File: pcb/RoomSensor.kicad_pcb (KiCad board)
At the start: 2 copper layers, 70 x 32 mm, 63 parts, among them J1 FH34SRJ-24S-0.5SH50, J2 USB_C_Receptacle_PowerOnly_6P, J3 programming, J4 external supply, Q1 SI1308EDL-T1-GE3, SW1 SW_Push, U1 ESP32-WROOM-32D, U2 DW01-P, U3 CEG8205A, U4 RT9080-33GJ5, U5 TP4056, U6 SCD40-D-R1, U7 SHT31-DIS, U8 BME680

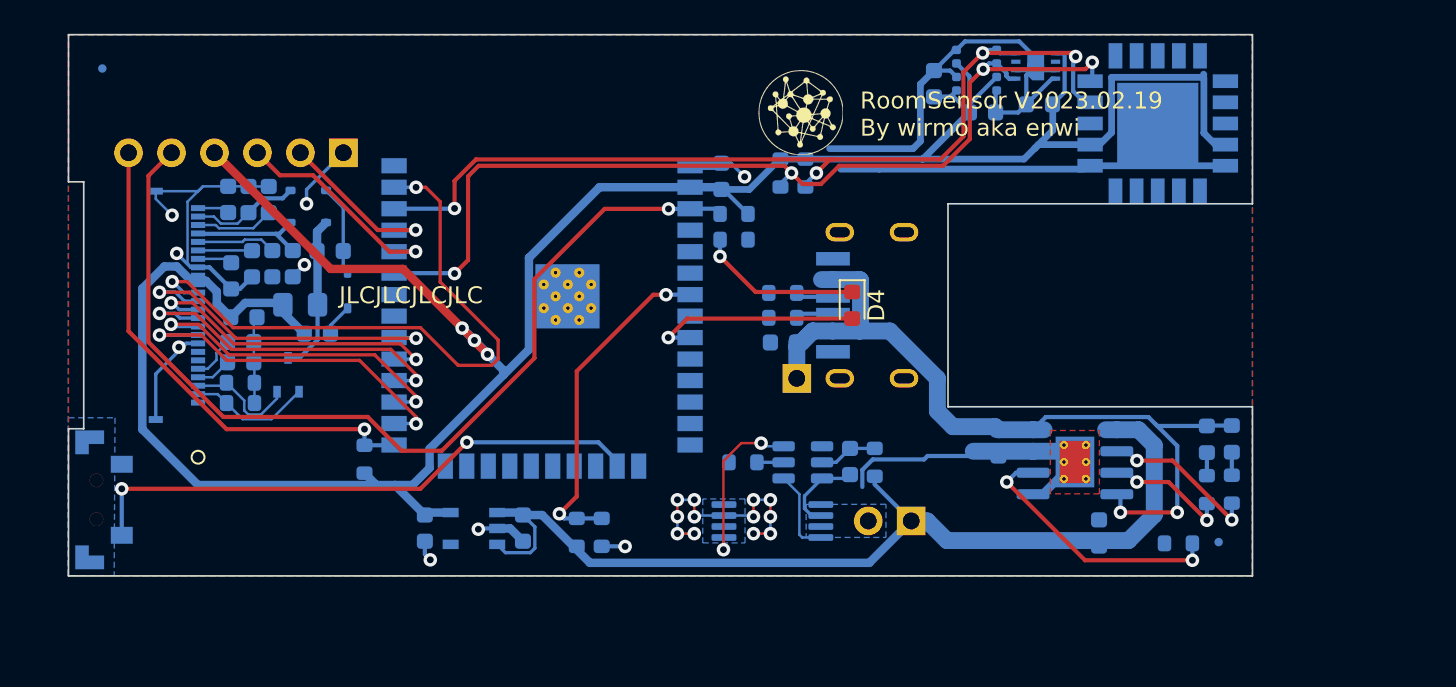
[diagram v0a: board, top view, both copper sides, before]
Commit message: Increase PCB size and fix EPD pinout
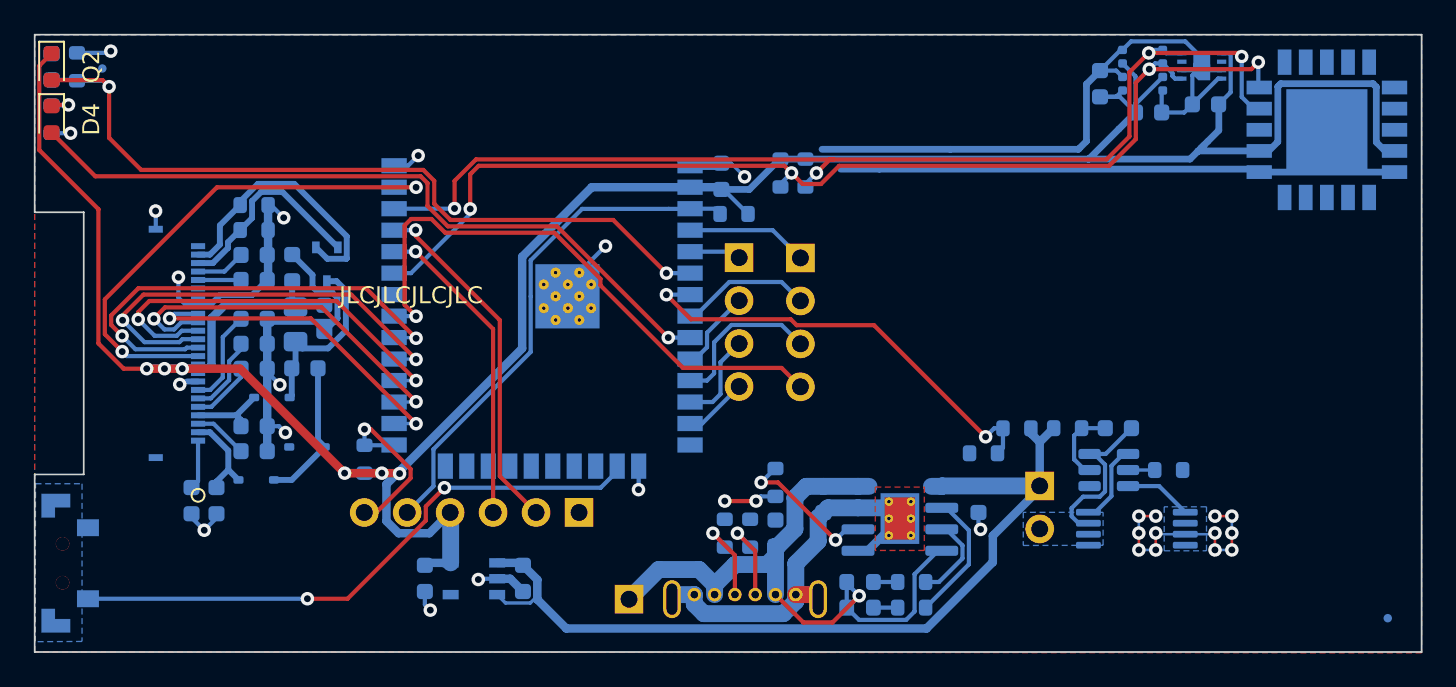
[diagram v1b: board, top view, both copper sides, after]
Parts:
- removed Ref**: Val**, Symbols_Custom:enwi_5mm
- added C15: 100n, Capacitor_SMD:C_0603_1608Metric, B.Cu at (-1.00, 1.90)
- added J5: Conn_01x04_Pin, Connector_PinHeader_2.54mm:PinHeader_1x04_P2.54mm_Vertical, B.Cu at (39.6, 13.2)
- added J6: Conn_01x04_Pin, Connector_PinHeader_2.54mm:PinHeader_1x04_P2.54mm_Vertical, B.Cu at (43.3, 13.2)
- added Q2: ALS-PT19-315C/L177/TR8, LED_SMD:LED_0603_1608Metric, F.Cu at (-1.00, 1.90)
- added R17: R_Small, Resistor_SMD:R_0603_1608Metric, B.Cu at (0.50, 1.90)
- C1, C10, C2, C3, C4, C5, C6, C7, C8, C9: value 1uF -> 1u
- C11, C12: value 4.7uF -> 4.7u
- C13: value 10uF -> 10u
- C16: value 0.1u -> 100n
- FID2: footprint Fiducial:Fiducial_0.5mm_Mask1mm -> Fiducial:Fiducial_0.5mm_Mask1.5mm
- J2: footprint Custom:TYPE-C-31-M-17_B -> Custom:TYPE-C 6P LCH10.0
- L1: value L_Small -> 68u
- moved D4 48.6 mm to (-1.00, 5.00)
- moved R11 41.0 mm to (-1.00, 5.00), turned to 90 degrees
- moved R9 26.7 mm to (56.1, 23.3), turned to 0 degrees
- moved J3 25.4 mm to (30.2, 28.2)
- moved R12 25.2 mm to (65.0, 25.7), turned to 0 degrees
- moved D6 24.1 mm to (46.8, 33.9), turned to 180 degrees
- moved R14 24.1 mm to (41.8, 26.5), turned to 90 degrees
- moved R10 23.1 mm to (54.1, 24.8), turned to 0 degrees
- moved D5 22.2 mm to (46.8, 32.4), turned to 180 degrees
- moved U3 21.6 mm to (63.2, 29.2), turned to 0 degrees
- moved R16 20.2 mm to (49.9, 33.9), turned to 180 degrees
- moved R15 18.3 mm to (49.9, 32.4), turned to 180 degrees
- moved J2 18.1 mm to (40.0, 31.5), turned to 0 degrees
- moved U2 18.1 mm to (61.5, 25.7), turned to 180 degrees
- moved C1 17.9 mm to (7.28, 27.6), turned to -90 degrees
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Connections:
- J1 pad 1: unconnected-(J1-Pad1) -> Net-(C1-Pad1)
- J1 pad 10: ESP_IO16 -> +3V3
- J1 pad 11: DC -> ESP_IO23
- J1 pad 12: CS -> CLK
- J1 pad 13: CLK -> CS
- J1 pad 14: ESP_IO23 -> DC
- J1 pad 15: +3V3 -> ESP_IO16
- J1 pad 16: +3V3 -> BUSY
- J1 pad 18: Net-(C4-Pad1) -> unconnected-(J1-Pad18)
- J1 pad 19: Net-(C9-Pad1) -> unconnected-(J1-Pad19)
- J1 pad 2: Net-(Q1-G) -> Net-(D2-A)
- J1 pad 20: Net-(C3-Pad1) -> Net-(C6-Pad1)
- J1 pad 21: Net-(D3-K) -> Net-(C10-Pad1)
- J1 pad 22: Net-(C2-Pad1) -> Net-(Q1-S)
- J1 pad 23: Net-(D2-A) -> Net-(Q1-G)
- J1 pad 24: Net-(C1-Pad1) -> unconnected-(J1-Pad24)
- J1 pad 3: Net-(Q1-S) -> Net-(C2-Pad1)
- J1 pad 4: Net-(C10-Pad1) -> Net-(D3-K)
- J1 pad 5: Net-(C6-Pad1) -> Net-(C3-Pad1)
- J1 pad 6: unconnected-(J1-Pad6) -> Net-(C9-Pad1)
- J1 pad 7: unconnected-(J1-Pad7) -> Net-(C4-Pad1)
- J1 pad 9: BUSY -> +3V3
- SW1 pad 3: (no net) -> -BATT
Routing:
- net ESP_IO34: track 0.00 -> 48.6 mm, vias 0 -> 2
- net -BATT: track 133.2 -> 170.7 mm, vias 21 -> 30
- net ESP_IO19: track 0.00 -> 34.9 mm, vias 0 -> 1
- net ESP_IO33: track 12.6 -> 43.6 mm
- net ESP_EN: track 57.0 -> 30.5 mm, vias 1 -> 0
- net ESP_IO0: track 29.6 -> 10.5 mm
- net +3V3: track 159.7 -> 172.1 mm, vias 3 -> 6
- net ESP_TX: track 9.99 -> 20.9 mm
- net ESP_IO22: track 55.3 -> 65.5 mm
- net ESP_IO26: track 0.00 -> 9.43 mm
- net Net-(Q1-G): track 7.26 -> 16.2 mm
- net ESP_IO21: track 57.2 -> 65.7 mm
- net +5V: track 49.2 -> 41.4 mm, vias 2 -> 1
- net ESP_IO32: track 0.00 -> 7.82 mm
- net Net-(D4-K): track 9.68 -> 2.04 mm
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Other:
- board size 70 x 32 mm -> 82 x 36.5 mm
- board text added: "IO 19|14"
- board text added: "IO 26|27"
- board text added: "IO 32|25"
- board text added: "IO 36|39"
- board text added: "RoomSensor V2023.02.25 By wirmo aka enwi"
- board text removed: "3V3"
- board text removed: "EN"
- board text removed: "GND"
- board text removed: "IO0"
- board text removed: "RX"
- board text removed: "RoomSensor V2023.02.19 By wirmo aka enwi"
- board text removed: "TX"

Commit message: Fix low power issues
- Fix spurious EPD wakeups by adding pull-up to EPD reset line
- Reduce power consumption by switching sensors off with mosfet
- Connect button to reset to reduce power by not needing rtc gpio
- Add solder jumper for silent boot
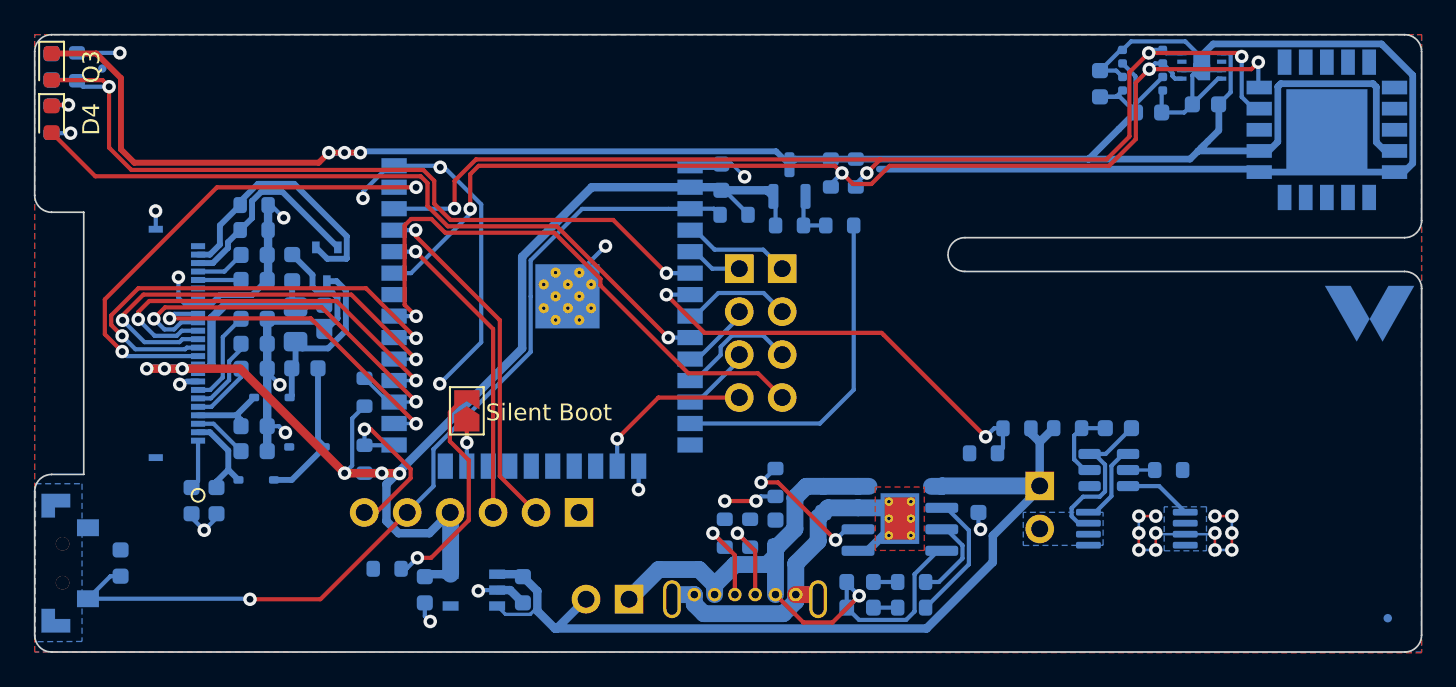
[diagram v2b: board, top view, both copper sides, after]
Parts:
- removed the J4 at (33.1, 33.4)
- added C15: 100n, Capacitor_SMD:C_0603_1608Metric, B.Cu at (3.08, 31.2)
- added J6: Conn_01x02_Pin, Connector_PinHeader_2.54mm:PinHeader_1x02_P2.54mm_Vertical, B.Cu at (33.1, 33.4)
- added JP1: silent boot, Jumper:SolderJumper-2_P1.3mm_Open_TrianglePad1.0x1.5mm, F.Cu at (23.6, 22.2)
- added Q2: AO3401A, Package_TO_SOT_SMD:SOT-23, B.Cu at (42.6, 8.62)
- added R15: 10k, Resistor_SMD:R_0603_1608Metric, B.Cu at (18.8, 31.6)
- added R5: 10k, Resistor_SMD:R_0603_1608Metric, B.Cu at (17.5, 21.1)
- added R6: 1k, Resistor_SMD:R_0603_1608Metric, B.Cu at (45.6, 11.3)
- added R7: 10k, Resistor_SMD:R_0603_1608Metric, B.Cu at (42.6, 11.3)
- added REF**: wirmo_small, Symbols_Custom:wirmo_small, B.Cu at (76.9, 16.5)
- FID1: footprint Fiducial:Fiducial_0.5mm_Mask1mm -> Fiducial:Fiducial_0.5mm_Mask1.5mm
- R21: renamed from R17; value R_Small -> 1k5
- moved R11 2.98 mm to (45.1, 8.18)
- moved R8 2.98 mm to (46.5, 8.18)
- moved J5 1.25 mm to (42.2, 13.8)
- moved U4 0.67 mm to (24.0, 32.8)
- moved C17 0.67 mm to (26.9, 32.8)
- moved C20 0.67 mm to (21.1, 32.8)
- moved J4 0.65 mm to (39.7, 13.8)
- moved C14 0.05 mm to (38.6, 8.43)
- moved R10 0.05 mm to (39.4, 10.7), turned to 180 degrees
- renumbered C15 to C21, C21 to C22, C22 to C23, C23 to C24, J5 to J4, J6 to J5, Q2 to Q3, R7 to R10, R8 to R11, R9 to R12, R10 to R13, R11 to R14, R12 to R16, R13 to R17, R14 to R18, R15 to R19, R16 to R20, R5 to R8, R6 to R9
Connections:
- C22 pad 1: +3V3 -> +3V3Sensors
- C23 pad 1: +3V3 -> +3V3Sensors
- C24 pad 1: +3V3 -> +3V3Sensors
- J4 pad 4: ESP_IO14 -> ESP_IO13
- Q3 pad 1: +3V3 -> +3V3Sensors
- R10 pad 1: ESP_EN -> +3V3
- R10 pad 2: +3V3 -> ESP_EN
- R11 pad 2: +3V3 -> +3V3Sensors
- R8 pad 2: +3V3 -> +3V3Sensors
- SW1 pad 2: ESP_IO13 -> ESP_EN
- SW1 pad 3: -BATT -> (no net)
- U1 pad 23: unconnected-(U1-IO15-Pad23) -> ESP_IO15
- U6 pad 19: +3V3 -> +3V3Sensors
- U6 pad 7: +3V3 -> +3V3Sensors
- U7 pad 5: +3V3 -> +3V3Sensors
- U8 pad 2: +3V3 -> +3V3Sensors
- U8 pad 6: +3V3 -> +3V3Sensors
- U8 pad 8: +3V3 -> +3V3Sensors
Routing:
- net +3V3Sensors: track 0.00 -> 115.9 mm, vias 0 -> 3
- net +3V3: track 172.1 -> 90.0 mm
- net ESP_IO13: track 35.6 -> 10.1 mm, vias 2 -> 1
- net ESP_EN: track 30.5 -> 54.1 mm, vias 0 -> 1
- net -BATT: track 170.7 -> 188.1 mm, vias 30 -> 32
- net ESP_IO14: track 3.81 -> 20.2 mm
- net Net-(JP1-B): track 0.00 -> 13.4 mm, vias 0 -> 1
- net Net-(Q2-G): track 0.00 -> 3.09 mm
- net ESP_IO15: track 0.00 -> 2.55 mm, vias 0 -> 1
- net ESP_IO16: track 22.5 -> 24.9 mm
- net ESP_IO26: track 9.43 -> 7.30 mm
- net ESP_IO32: track 7.82 -> 6.47 mm
- net ESP_IO27: track 5.43 -> 4.26 mm
- net +BATT: track 54.9 -> 55.7 mm
- net ESP_SEN_VP: track 7.20 -> 6.39 mm
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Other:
- outline, holes or cut-outs redrawn
- board text added: "0"
- board text added: "BV"
- board text added: "EN"
- board text added: "G"
- board text added: "IO 19|16"
- board text added: "RX"
- board text added: "RoomSensor V2023.04.01 by wirmo aka enwi"
- board text added: "Silent Boot"
- board text added: "TX"
- board text added: "V"
- board text removed: "IO 19|14"
- board text removed: "RoomSensor V2023.02.25 By wirmo aka enwi"

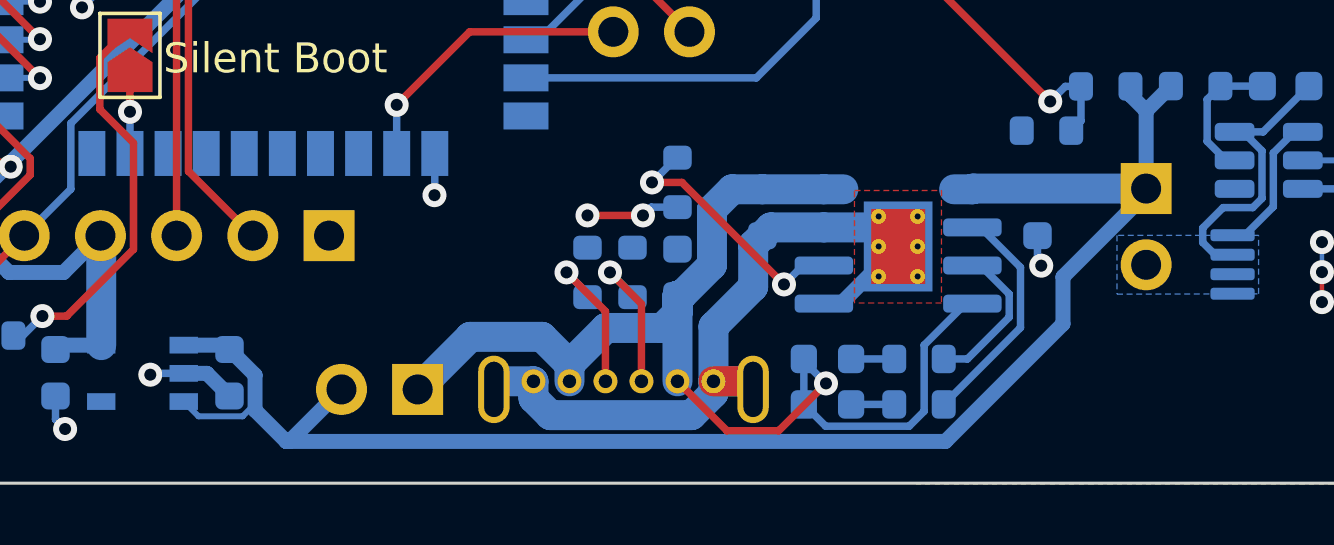
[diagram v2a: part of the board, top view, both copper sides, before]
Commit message: Replace b- net with -Battery
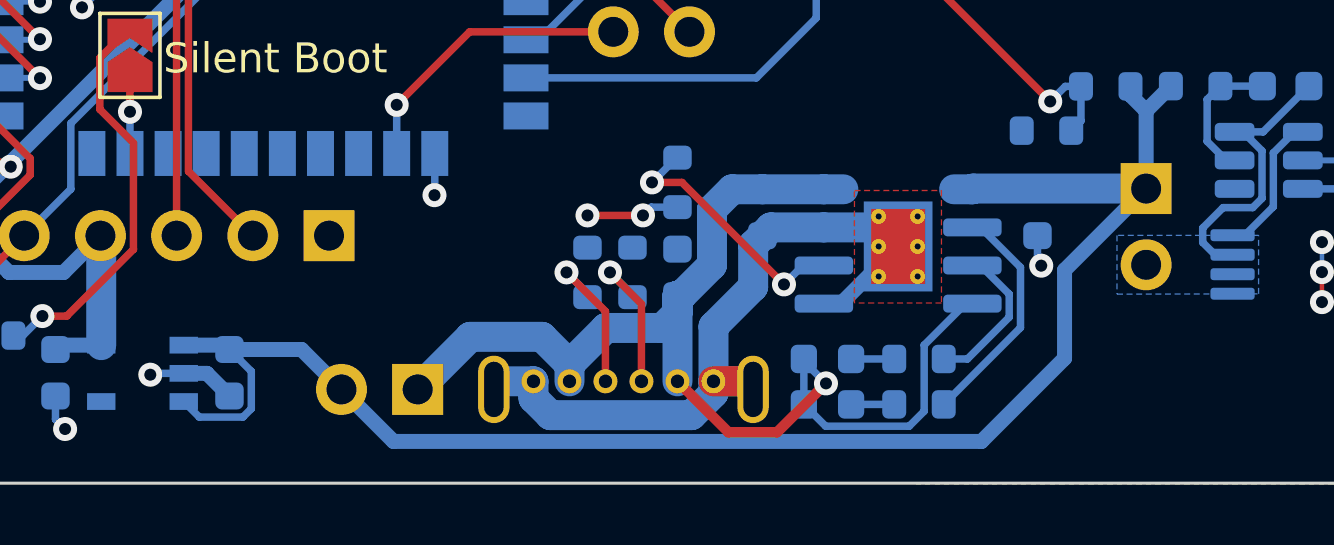
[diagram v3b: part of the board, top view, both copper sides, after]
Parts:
- R12, R13: value 47k -> 1M
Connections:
- BT1 pad 2: b- -> -BATT
- C1 pad 2: -BATT -> GND
- C10 pad 2: -BATT -> GND
- C12 pad 1: -BATT -> GND
- C13 pad 1: -BATT -> GND
- C14 pad 2: -BATT -> GND
- C15 pad 2: -BATT -> GND
- C16 pad 1: b- -> -BATT
- C17 pad 2: -BATT -> GND
- C18 pad 2: -BATT -> GND
- C19 pad 2: -BATT -> GND
- C2 pad 2: -BATT -> GND
- C20 pad 2: -BATT -> GND
- C21 pad 2: -BATT -> GND
- C22 pad 2: -BATT -> GND
- C23 pad 2: -BATT -> GND
- C24 pad 2: -BATT -> GND
- C3 pad 2: -BATT -> GND
- C4 pad 2: -BATT -> GND
- C5 pad 2: -BATT -> GND
- C6 pad 2: -BATT -> GND
- C7 pad 2: -BATT -> GND
- C8 pad 2: -BATT -> GND
- C9 pad 2: -BATT -> GND
- D1 pad 1: -BATT -> GND
- J1 pad 17: -BATT -> GND
- J1 pad 25: -BATT -> GND
- J1 pad 26: -BATT -> GND
- J1 pad 8: -BATT -> GND
- J2 pad A12: -BATT -> GND
- J2 pad S1: -BATT -> GND
- J3 pad 1: -BATT -> GND
- R1 pad 2: -BATT -> GND
- R13 pad 1: -BATT -> GND
- R14 pad 1: -BATT -> GND
- R15 pad 2: -BATT -> GND
- R16 pad 2: -BATT -> GND
- R18 pad 1: -BATT -> GND
- R2 pad 2: -BATT -> GND
- R21 pad 2: -BATT -> GND
- R3 pad 1: -BATT -> GND
- R4 pad 1: -BATT -> GND
- SW1 pad 1: -BATT -> GND
- U1 pad 1: -BATT -> GND
- U1 pad 15: -BATT -> GND
- U1 pad 38: -BATT -> GND
- U1 pad 39: -BATT -> GND
- U2 pad 6: b- -> -BATT
- U3 pad 2: b- -> -BATT
- U3 pad 3: b- -> -BATT
- U3 pad 6: -BATT -> GND
- U3 pad 7: -BATT -> GND
- U4 pad 2: -BATT -> GND
- U5 pad 1: -BATT -> GND
- U5 pad 3: -BATT -> GND
- U5 pad 9: -BATT -> GND
- U6 pad 20: -BATT -> GND
- U6 pad 21: -BATT -> GND
- U6 pad 6: -BATT -> GND
- U7 pad 2: -BATT -> GND
- U7 pad 7: -BATT -> GND
- U7 pad 8: -BATT -> GND
- U7 pad 9: -BATT -> GND
- U8 pad 1: -BATT -> GND
- U8 pad 5: -BATT -> GND
- U8 pad 7: -BATT -> GND
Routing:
- net GND: track 0.00 -> 188.1 mm, vias 0 -> 32
- net -BATT: track 188.1 -> 10.5 mm, vias 32 -> 0
- net b-: track 10.5 -> 0.00 mm
- net +BATT: track 55.7 -> 54.9 mm
- added copper zone on B.Cu, net GND
- added copper zone on F.Cu, net GND
- removed copper zone on B.Cu, net b-
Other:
- board text added: "RoomSensor V2023.07.30 by wirmo aka enwi"
- board text removed: "RoomSensor V2023.04.01 by wirmo aka enwi"
